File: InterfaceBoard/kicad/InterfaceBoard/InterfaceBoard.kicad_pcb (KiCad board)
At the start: 2 copper layers, 60.2 x 73.4 mm, 45 parts, among them J10 JST Portamento Pot, J3 JST MIDI IN, J5 JST MIDI THRU, J6 JST GATE IN, J7 JST GATE CTRL, J8 JST Pitch Adj., J9 JST PWR, Q1 2N7000, Q2 2N7000, Q3 2N7000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

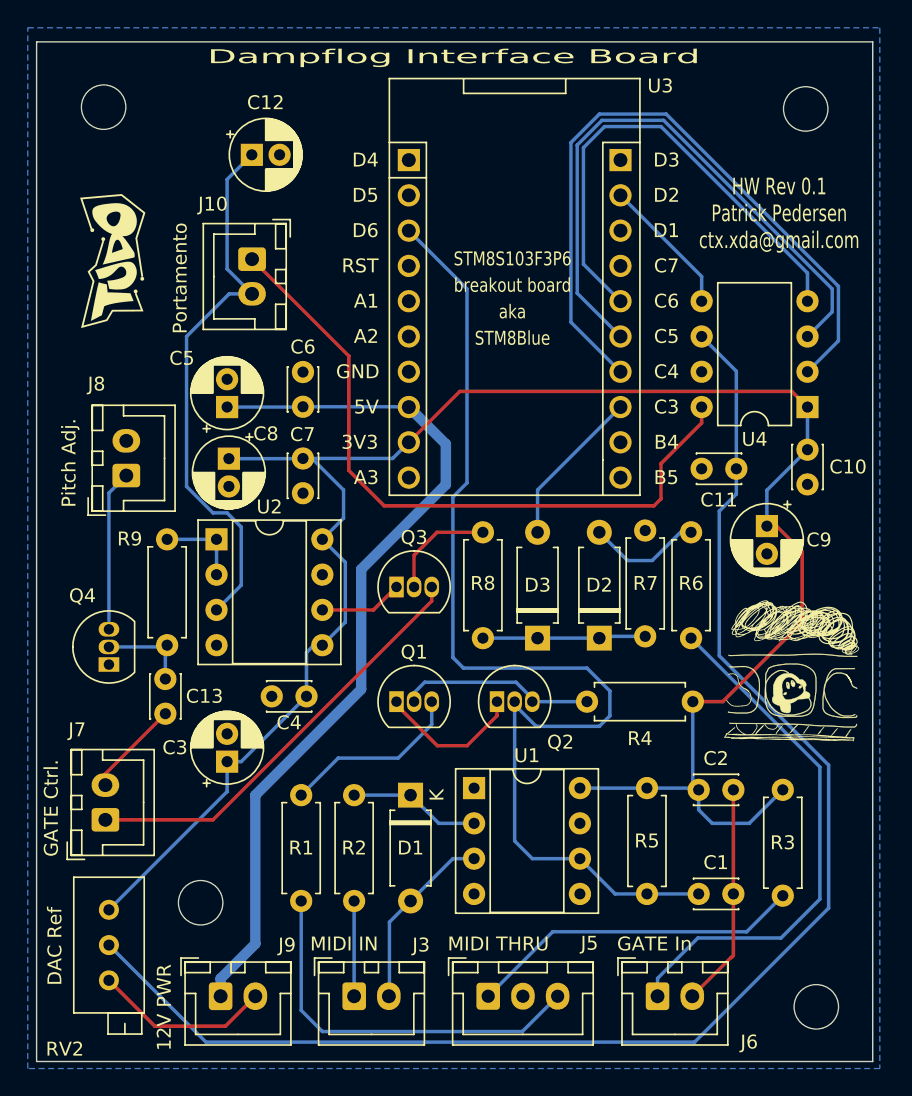
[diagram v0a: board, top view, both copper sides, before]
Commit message: Interface Board: Kicad: Minor fixes regarding JST connector orientation
Signed-off-by: CTXz <ctx.xda@gmail.com>
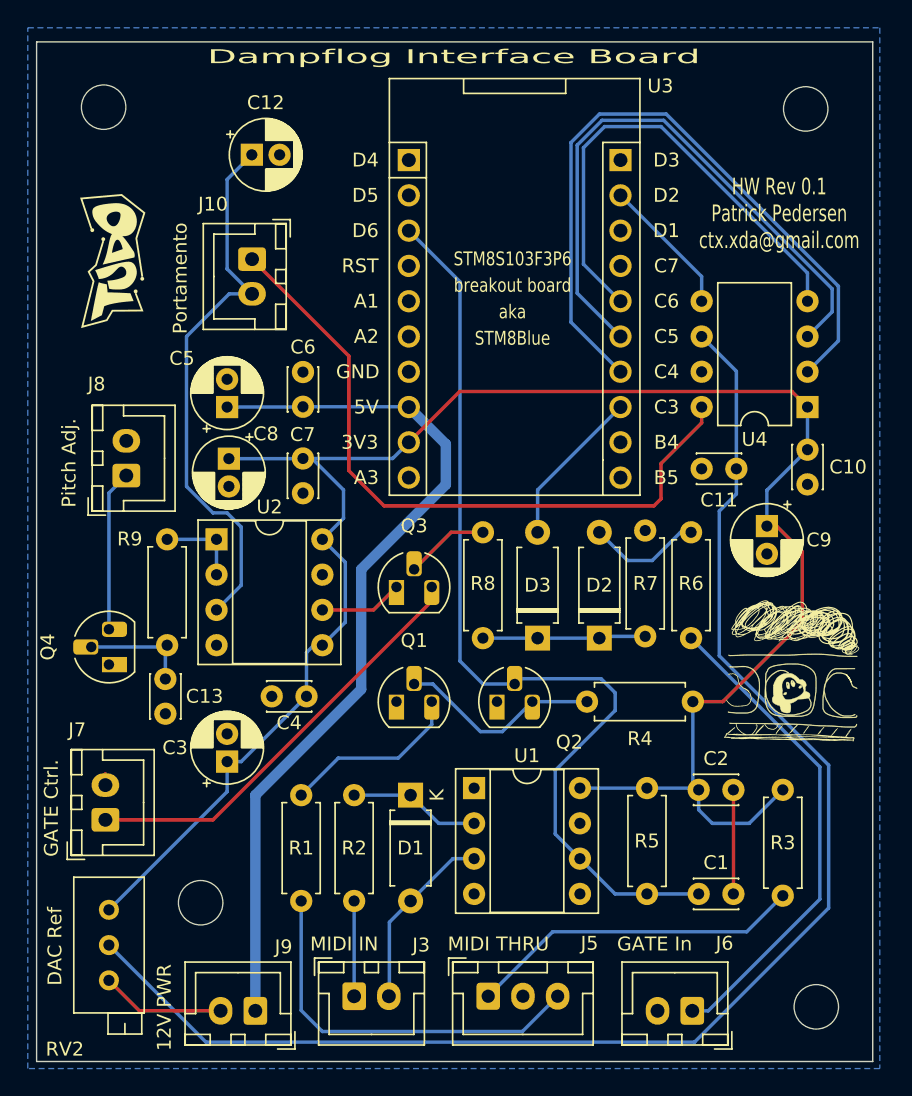
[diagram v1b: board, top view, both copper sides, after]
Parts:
- Q1, Q2, Q3, Q4: footprint Package_TO_SOT_THT:TO-92_Inline -> Package_TO_SOT_THT:TO-92_HandSolder
- moved J6 2.71 mm to (120.4, 130.8), turned to 180 degrees
- moved J9 2.71 mm to (88.9, 130.8), turned to 180 degrees
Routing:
- net GND: track 52.5 -> 23.3 mm
- net MIDI IN DATA: track 79.9 -> 69.0 mm
- net GATE JACK: track 38.0 -> 35.1 mm
- net Net-(Q3-G): track 7.92 -> 6.06 mm
- net /CV: track 6.55 -> 7.82 mm
- net Net-(Q1-G): track 14.1 -> 15.0 mm
